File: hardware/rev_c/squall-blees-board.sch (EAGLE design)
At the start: 18 parts, among them J1 SQUALL_HEADER, J4 HIROSE-DF40C-10DP-0.4V, J5 HIROSE-DF40C-10DP-0.4V

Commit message: Second pass at Rev C of BLEES. Added accelerometer
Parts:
- removed 9DOF: MPU-9250, chips:MPU-9250
- removed C5, C7: 0.1uF, passives:CAPACITOR
- removed C6: 10nF, passives:CAPACITOR
- added C10, C8: 0.1uF, passives:CAPACITOR
- added U1: ADXL362, SparkFun-Sensors:ADXL362
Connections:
- removed net N$1: 9DOF.REGOUT, C7.1
- net A5: now also U1.!CS
- net A6: now also U1.INT2; no longer 9DOF.INT
- net A7: now also U1.INT1; no longer LIGHT.INT
- net GND: now also C10.2, C8.2, U1.GND; no longer 9DOF.AD0/MISO, 9DOF.FSYNC, 9DOF.GND, C5.2, C6.2, C7.2
- net MISO: now also U1.MISO
- net MOSI: now also U1.MOSI
- net P22: now also LIGHT.INT
- net SCL: no longer 9DOF.SCLK
- net SCLK: now also U1.SCLK
- net SDA: no longer 9DOF.SDA/MOSI
- net VCC: now also C10.1, C8.1, U1.VDDIO, U1.VS; no longer 9DOF.!CS, 9DOF.VDD, 9DOF.VDDIO, C5.1, C6.1

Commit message: Panelized version of rev C BLEES
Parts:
- removed C10: 0.1uF, passives:CAPACITOR
- removed PRESSURE: LPS331APQFN, blees:LPS331APQFN
- added C6: 10uF, passives:CAPACITOR0603_CAP
- added U4: ADXL362, SparkFun-Sensors:ADXL362
- C1: value 10uF -> 100nF; device passives:CAPACITOR0603_CAP -> passives:CAPACITOR
- C4: value 100nF -> 0.1uF
- R1: value 2kΩ -> 1kΩ
- R3: value 1kΩ -> 2kΩ
- U1: value ADXL362 -> LPS331APQFN; device SparkFun-Sensors:ADXL362 -> blees:LPS331APQFN
- renumbered C8 to C5, J4 to J2, J5 to J3, LIGHT to U2, TEMP/HUMID to U3
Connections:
- net A5: now also U4.!CS; no longer U1.!CS
- net A6: now also U4.INT2; no longer U1.INT2
- net A7: now also U4.INT1; no longer U1.INT1
- net GND: now also C6.2, U1.GND@12, U1.GND@13, U1.GND@16, U1.GND@5, U1.RSV, U1.SA0, U4.GND; no longer C10.2, PRESSURE.GND@12, PRESSURE.GND@13, PRESSURE.GND@16, PRESSURE.GND@5, PRESSURE.RSV, PRESSURE.SA0, U1.GND
- net MISO: now also U4.MISO; no longer U1.MISO
- net MOSI: now also U4.MOSI; no longer U1.MOSI
- net N$2: now also R1.1; no longer R3.1
- net P23: now also U1.INT2; no longer PRESSURE.INT2
- net P24: now also U1.INT1; no longer PRESSURE.INT1
- net SCL: now also U1.SCL; no longer PRESSURE.SCL
- net SCLK: now also U4.SCLK; no longer U1.SCLK
- net SDA: now also R3.1, U1.SDA; no longer PRESSURE.SDA, R1.1
- net VCC: now also C6.1, U1.CS, U1.VCCA, U1.VDD, U1.VDD_IO, U4.VDDIO, U4.VS; no longer C10.1, PRESSURE.CS, PRESSURE.VCCA, PRESSURE.VDD, PRESSURE.VDD_IO, U1.VDDIO, U1.VS
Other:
- note added: "Acceleration"
- note added: "Light"
- note added: "Pressure"
- note added: "Temp/Humid"
- moved on the sheet: C1, C2, C4, R1, R3

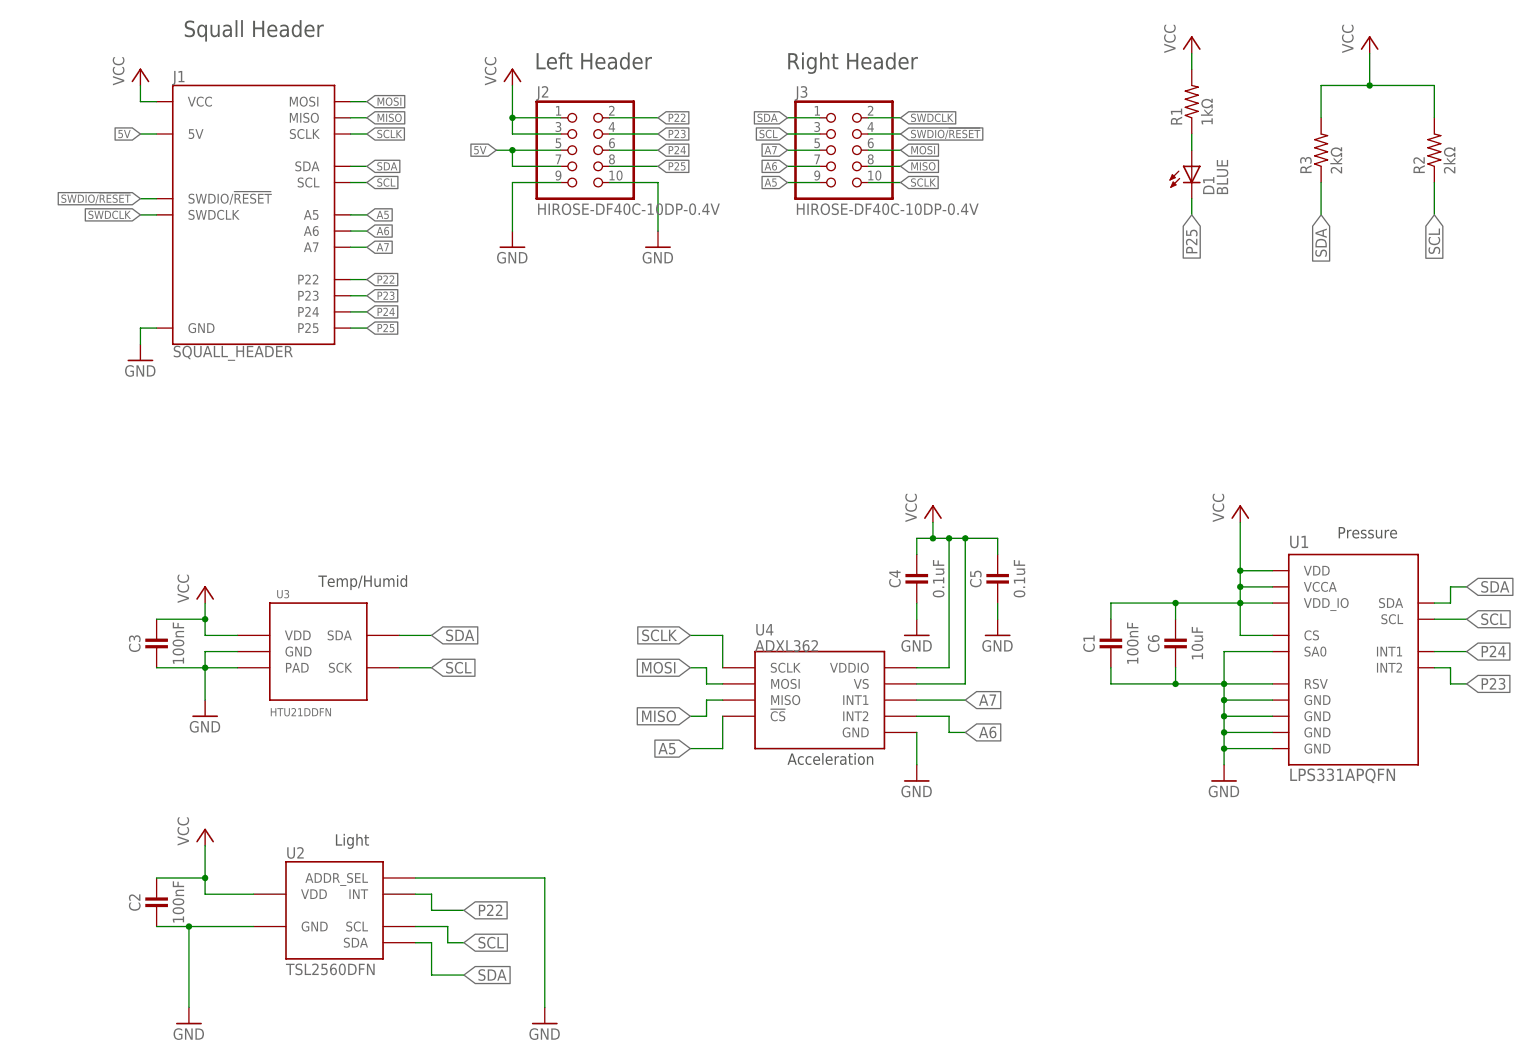
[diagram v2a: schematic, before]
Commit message: Swapped out temp/humidity sensor
This one is lower power, same functionality, and purchasable
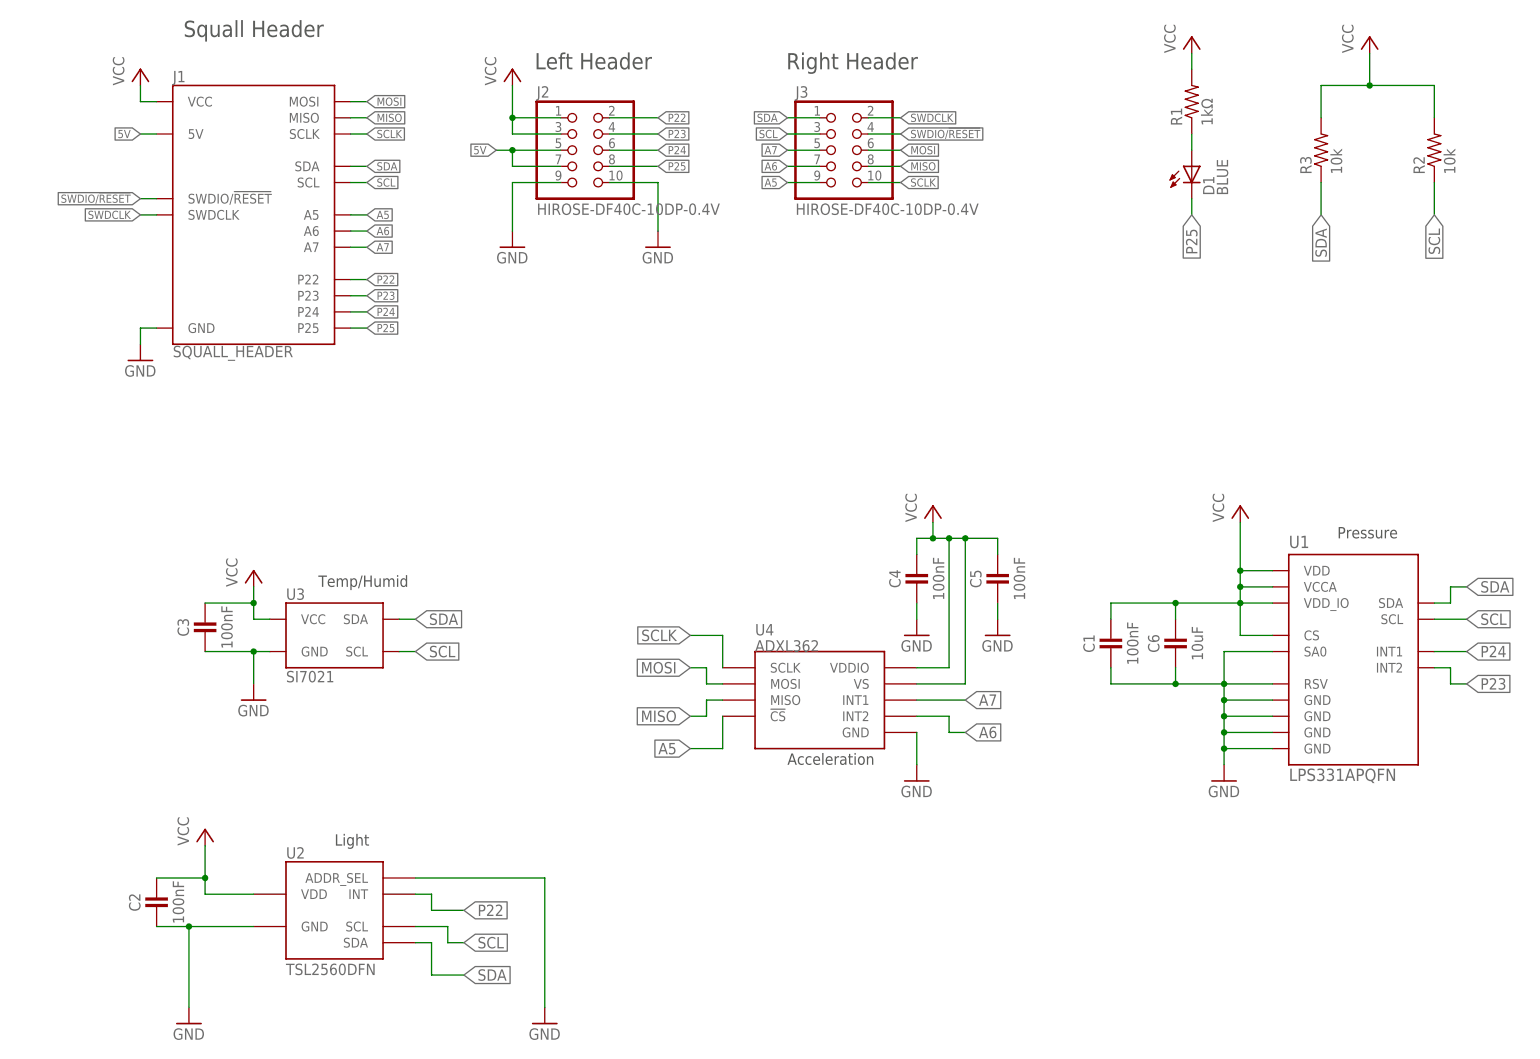
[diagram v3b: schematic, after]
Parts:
- C4, C5: value 0.1uF -> 100nF
- R2, R3: value 2kΩ -> 10k
- U3: value HTU21DDFN -> SI7021; device blees:HTU21DDFN -> chips:SI7021
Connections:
- net GND: no longer U3.PAD
- net SCL: now also U3.SCL; no longer U3.SCK
- net VCC: now also U3.VCC; no longer U3.VDD
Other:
- moved on the sheet: C3
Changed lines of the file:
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@@
 <part name="P+4" library="supply1" deviceset="VCC" device=""/>
 <part name="GND9" library="supply1" deviceset="GND" device=""/>
-<part name="U3" library="blees" deviceset="HTU21D" device="DFN"/>
 <part name="U2" library="blees" deviceset="TSL2560" device="DFN"/>
 <part name="GND2" library="umich" deviceset="GND" device=""/>
@@
 <part name="C3" library="passives" deviceset="CAPACITOR" device="" value="100nF"/>
 <part name="C2" library="passives" deviceset="CAPACITOR" device="" value="100nF"/>
-<part name="R3" library="passives" deviceset="RESISTOR" device="0402_RES" value="2kΩ"/>
+<part name="R3" library="passives" deviceset="RESISTOR" device="0402_RES" value="10k"/>
 <part name="P+6" library="supply1" deviceset="VCC" device=""/>
-<part name="R2" library="passives" deviceset="RESISTOR" device="0402_RES" value="2kΩ"/>
+<part name="R2" library="passives" deviceset="RESISTOR" device="0402_RES" value="10k"/>
 <part name="D1" library="SparkFun-LED" deviceset="LED" device="0603" value="BLUE"/>
 <part name="R1" library="passives" deviceset="RESISTOR" device="0402_RES" value="1kΩ"/>
@@
 <part name="GND15" library="umich" deviceset="GND" device=""/>
 <part name="P+11" library="supply1" deviceset="VCC" device=""/>
-<part name="C4" library="passives" deviceset="CAPACITOR" device="" value="0.1uF"/>
-<part name="C5" library="passives" deviceset="CAPACITOR" device="" value="0.1uF"/>
+<part name="C4" library="passives" deviceset="CAPACITOR" device="" value="100nF"/>
+<part name="C5" library="passives" deviceset="CAPACITOR" device="" value="100nF"/>
 <part name="GND16" library="umich" deviceset="GND" device=""/>
+<part name="U3" library="chips" deviceset="SI7021" device=""/>
 </parts>
 <sheets>
@@
 <instance part="P+4" gate="VCC" x="81.28" y="170.18"/>
 <instance part="GND9" gate="1" x="104.14" y="142.24"/>
-<instance part="U3" gate="U1" x="50.8" y="78.74"/>
 <instance part="U2" gate="U1" x="53.34" y="38.1"/>
-<instance part="GND2" gate="1" x="33.02" y="68.58"/>
-<instance part="P+2" gate="VCC" x="33.02" y="88.9"/>
+<instance part="GND2" gate="1" x="40.64" y="71.12"/>
+<instance part="P+2" gate="VCC" x="40.64" y="91.44"/>
 <instance part="P+3" gate="VCC" x="33.02" y="50.8"/>
 <instance part="P+5" gate="VCC" x="195.58" y="101.6"/>
@@
 <instance part="C6" gate="G$1" x="185.42" y="81.28"/>
 <instance part="C1" gate="G$1" x="175.26" y="81.28"/>
-<instance part="C3" gate="G$1" x="25.4" y="81.28"/>
+<instance part="C3" gate="G$1" x="33.02" y="83.82"/>
 <instance part="C2" gate="G$1" x="25.4" y="40.64"/>
 <instance part="R3" gate="G$1" x="208.28" y="157.48" rot="R90"/>
@@
 <instance part="C5" gate="G$1" x="157.48" y="91.44"/>
 <instance part="GND16" gate="1" x="144.78" y="58.42"/>
+<instance part="U3" gate="G$1" x="53.34" y="81.28"/>
 </instances>
 <busses>
@@
 </segment>
 <segment>
-<pinref part="U3" gate="U1" pin="VDD"/>
 <pinref part="P+2" gate="VCC" pin="VCC"/>
-<wire x1="38.1" y1="81.28" x2="33.02" y2="81.28" width="0.1524" layer="91"/>
-<wire x1="33.02" y1="81.28" x2="33.02" y2="83.82" width="0.1524" layer="91"/>
+<wire x1="40.64" y1="83.82" x2="40.64" y2="86.36" width="0.1524" layer="91"/>
 <pinref part="C3" gate="G$1" pin="1"/>
-<wire x1="33.02" y1="83.82" x2="33.02" y2="86.36" width="0.1524" layer="91"/>
-<wire x1="25.4" y1="83.82" x2="33.02" y2="83.82" width="0.1524" layer="91"/>
-<junction x="33.02" y="83.82"/>
+<wire x1="40.64" y1="86.36" x2="40.64" y2="88.9" width="0.1524" layer="91"/>
+<wire x1="33.02" y1="86.36" x2="40.64" y2="86.36" width="0.1524" layer="91"/>
+<junction x="40.64" y="86.36"/>
+<pinref part="U3" gate="G$1" pin="VCC"/>
+<wire x1="40.64" y1="83.82" x2="43.18" y2="83.82" width="0.1524" layer="91"/>
 </segment>
 <segment>
@@
 </segment>
 <segment>
-<pinref part="U3" gate="U1" pin="GND"/>
 <pinref part="GND2" gate="1" pin="GND"/>
-<wire x1="38.1" y1="78.74" x2="33.02" y2="78.74" width="0.1524" layer="91"/>
-<wire x1="33.02" y1="78.74" x2="33.02" y2="76.2" width="0.1524" layer="91"/>
-<pinref part="U3" gate="U1" pin="PAD"/>
-<wire x1="33.02" y1="76.2" x2="33.02" y2="71.12" width="0.1524" layer="91"/>
-<wire x1="38.1" y1="76.2" x2="33.02" y2="76.2" width="0.1524" layer="91"/>
-<junction x="33.02" y="76.2"/>
+<wire x1="40.64" y1="78.74" x2="40.64" y2="73.66" width="0.1524" layer="91"/>
 <pinref part="C3" gate="G$1" pin="2"/>
-<wire x1="25.4" y1="76.2" x2="33.02" y2="76.2" width="0.1524" layer="91"/>
+<wire x1="33.02" y1="78.74" x2="40.64" y2="78.74" width="0.1524" layer="91"/>
+<pinref part="U3" gate="G$1" pin="GND"/>
+<wire x1="40.64" y1="78.74" x2="43.18" y2="78.74" width="0.1524" layer="91"/>
+<junction x="40.64" y="78.74"/>
 </segment>
 <segment>
@@
 </segment>
 <segment>
-<pinref part="U3" gate="U1" pin="SDA"/>
-<wire x1="63.5" y1="81.28" x2="68.58" y2="81.28" width="0.1524" layer="91"/>
-<label x="68.58" y="81.28" size="1.778" layer="95" xref="yes"/>
+<label x="66.04" y="83.82" size="1.778" layer="95" xref="yes"/>
+<pinref part="U3" gate="G$1" pin="SDA"/>
+<wire x1="63.5" y1="83.82" x2="66.04" y2="83.82" width="0.1524" layer="91"/>
 </segment>
 <segment>
@@
 </segment>
 <segment>
-<pinref part="U3" gate="U1" pin="SCK"/>
-<wire x1="63.5" y1="76.2" x2="68.58" y2="76.2" width="0.1524" layer="91"/>
-<label x="68.58" y="76.2" size="1.778" layer="95" xref="yes"/>
-</segment>
-<segment>
+<label x="66.04" y="78.74" size="1.778" layer="95" xref="yes"/>
+<pinref part="U3" gate="G$1" pin="SCL"/>
+<wire x1="63.5" y1="78.74" x2="66.04" y2="78.74" width="0.1524" layer="91"/>
+</segment>
+<segment>
